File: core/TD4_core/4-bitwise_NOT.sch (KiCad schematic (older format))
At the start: 2 parts, among them U3 74HC04

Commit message: Decoder done (finally!)
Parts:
- renumbered C2 to C17, U3 to U17

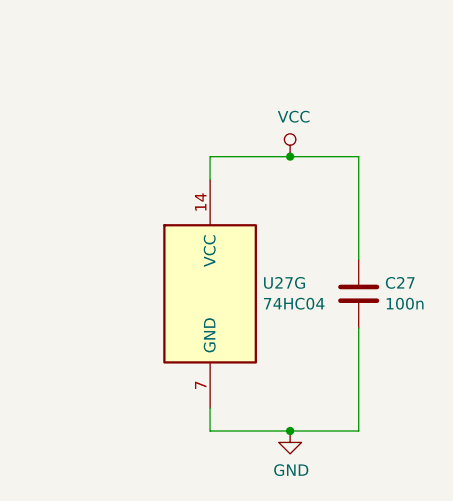
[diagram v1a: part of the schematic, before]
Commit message: Core schematic done. Backplane connector added, including separate .sch file to append.
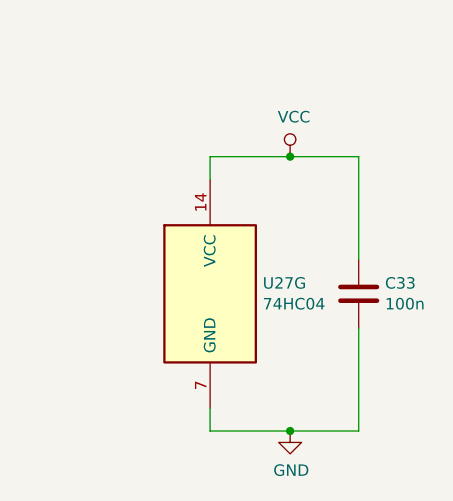
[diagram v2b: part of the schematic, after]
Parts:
- C23: renamed from C17; footprint (none) -> Capacitor_SMD:C_0805_2012Metric
- U17: footprint (none) -> Package_SO:SOIC-14_3.9x8.7mm_P1.27mm
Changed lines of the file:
@@
 encoding utf-8
 Sheet 6 23
-Title ""
+Title "TD4 core module"
 Date ""
-Rev ""
+Rev "v1.0"
 Comp ""
 Comment1 ""
@@
 F 0 "U27" H 5100 2617 50  0000 C CNN
 F 1 "74HC04" H 5100 2526 50  0000 C CNN
-F 2 "" H 5100 2300 50  0001 C CNN
+F 2 "Package_SO:SOIC-14_3.9x8.7mm_P1.27mm" H 5100 2300 50  0001 C CNN
 F 3 "http://www.nxp.com/documents/data_sheet/74HC_HCT04.pdf" H 5100 2300 50  0001 C CNN
 	1    5100 2300
@@
 F 0 "U27" H 5100 3117 50  0000 C CNN
 F 1 "74HC04" H 5100 3026 50  0000 C CNN
-F 2 "" H 5100 2800 50  0001 C CNN
+F 2 "Package_SO:SOIC-14_3.9x8.7mm_P1.27mm" H 5100 2800 50  0001 C CNN
 F 3 "http://www.nxp.com/documents/data_sheet/74HC_HCT04.pdf" H 5100 2800 50  0001 C CNN
 	2    5100 2800
@@
 F 0 "U27" H 5100 3617 50  0000 C CNN
 F 1 "74HC04" H 5100 3526 50  0000 C CNN
-F 2 "" H 5100 3300 50  0001 C CNN
+F 2 "Package_SO:SOIC-14_3.9x8.7mm_P1.27mm" H 5100 3300 50  0001 C CNN
 F 3 "http://www.nxp.com/documents/data_sheet/74HC_HCT04.pdf" H 5100 3300 50  0001 C CNN
 	3    5100 3300
@@
 F 0 "U27" H 5100 4117 50  0000 C CNN
 F 1 "74HC04" H 5100 4026 50  0000 C CNN
-F 2 "" H 5100 3800 50  0001 C CNN
+F 2 "Package_SO:SOIC-14_3.9x8.7mm_P1.27mm" H 5100 3800 50  0001 C CNN
 F 3 "http://www.nxp.com/documents/data_sheet/74HC_HCT04.pdf" H 5100 3800 50  0001 C CNN
 	4    5100 3800
@@
 F 0 "U27" H 5100 4617 50  0000 C CNN
 F 1 "74HC04" H 5100 4526 50  0000 C CNN
-F 2 "" H 5100 4300 50  0001 C CNN
+F 2 "Package_SO:SOIC-14_3.9x8.7mm_P1.27mm" H 5100 4300 50  0001 C CNN
 F 3 "http://www.nxp.com/documents/data_sheet/74HC_HCT04.pdf" H 5100 4300 50  0001 C CNN
 	5    5100 4300
@@
 F 0 "U27" H 5100 5117 50  0000 C CNN
 F 1 "74HC04" H 5100 5026 50  0000 C CNN
-F 2 "" H 5100 4800 50  0001 C CNN
+F 2 "Package_SO:SOIC-14_3.9x8.7mm_P1.27mm" H 5100 4800 50  0001 C CNN
 F 3 "http://www.nxp.com/documents/data_sheet/74HC_HCT04.pdf" H 5100 4800 50  0001 C CNN
 	6    5100 4800
@@
 F 0 "U27" H 8430 5646 50  0000 L CNN
 F 1 "74HC04" H 8430 5555 50  0000 L CNN
-F 2 "" H 8200 5600 50  0001 C CNN
+F 2 "Package_SO:SOIC-14_3.9x8.7mm_P1.27mm" H 8200 5600 50  0001 C CNN
 F 3 "http://www.nxp.com/documents/data_sheet/74HC_HCT04.pdf" H 8200 5600 50  0001 C CNN
 	7    8200 5600
@@
 AR Path="/5C5DC05E/5CD1F07F/5C820D48" Ref="C?"  Part="1"
 AR Path="/5C5DC05E/5CD1F083/5C820D48" Ref="C?"  Part="1"
-AR Path="/5C594F41/5C6679B7/5C820D48" Ref="C17"  Part="1"
+AR Path="/5C594F41/5C6679B7/5C820D48" Ref="C23"  Part="1"
 AR Path="/5C594F41/5C66DBE0/5C820D48" Ref="C?"  Part="1"
-AR Path="/5C594F41/5C66DBF5/5C820D48" Ref="C20"  Part="1"
-AR Path="/5C594F41/5C66DC0A/5C820D48" Ref="C22"  Part="1"
-AR Path="/5C594F41/5C66DC28/5C820D48" Ref="C24"  Part="1"
-AR Path="/5C594F41/5C67520B/5C820D48" Ref="C27"  Part="1"
+AR Path="/5C594F41/5C66DBF5/5C820D48" Ref="C26"  Part="1"
+AR Path="/5C594F41/5C66DC0A/5C820D48" Ref="C28"  Part="1"
+AR Path="/5C594F41/5C66DC28/5C820D48" Ref="C30"  Part="1"
+AR Path="/5C594F41/5C67520B/5C820D48" Ref="C33"  Part="1"
 AR Path="/5C594F41/5C691BDA/5C820D48" Ref="C?"  Part="1"
-F 0 "C27" H 8965 5646 50  0000 L CNN
+F 0 "C33" H 8965 5646 50  0000 L CNN
 F 1 "100n" H 8965 5555 50  0000 L CNN
-F 2 "" H 8888 5450 50  0001 C CNN
+F 2 "Capacitor_SMD:C_0805_2012Metric" H 8888 5450 50  0001 C CNN
 F 3 "~" H 8850 5600 50  0001 C CNN
 	1    8850 5600
@@
 AR Path="/5C5DC05E/5CD1F07F/5C820E22" Ref="#PWR?"  Part="1"
 AR Path="/5C5DC05E/5CD1F083/5C820E22" Ref="#PWR?"  Part="1"
-AR Path="/5C594F41/5C6679B7/5C820E22" Ref="#PWR060"  Part="1"
+AR Path="/5C594F41/5C6679B7/5C820E22" Ref="#PWR074"  Part="1"
 AR Path="/5C594F41/5C66DBE0/5C820E22" Ref="#PWR?"  Part="1"
-AR Path="/5C594F41/5C66DBF5/5C820E22" Ref="#PWR068"  Part="1"
-AR Path="/5C594F41/5C66DC0A/5C820E22" Ref="#PWR074"  Part="1"
-AR Path="/5C594F41/5C66DC28/5C820E22" Ref="#PWR080"  Part="1"
-AR Path="/5C594F41/5C67520B/5C820E22" Ref="#PWR088"  Part="1"
+AR Path="/5C594F41/5C66DBF5/5C820E22" Ref="#PWR082"  Part="1"
+AR Path="/5C594F41/5C66DC0A/5C820E22" Ref="#PWR088"  Part="1"
+AR Path="/5C594F41/5C66DC28/5C820E22" Ref="#PWR094"  Part="1"
+AR Path="/5C594F41/5C67520B/5C820E22" Ref="#PWR0102"  Part="1"
 AR Path="/5C594F41/5C691BDA/5C820E22" Ref="#PWR?"  Part="1"
-F 0 "#PWR088" H 8550 5950 50  0001 C CNN
+F 0 "#PWR0102" H 8550 5950 50  0001 C CNN
 F 1 "GND" H 8555 6027 50  0000 C CNN
 F 2 "" H 8550 6200 50  0001 C CNN
@@
 AR Path="/5C5DC05E/5CD1F07F/5C820E73" Ref="#PWR?"  Part="1"
 AR Path="/5C5DC05E/5CD1F083/5C820E73" Ref="#PWR?"  Part="1"
-AR Path="/5C594F41/5C6679B7/5C820E73" Ref="#PWR059"  Part="1"
+AR Path="/5C594F41/5C6679B7/5C820E73" Ref="#PWR073"  Part="1"
 AR Path="/5C594F41/5C66DBE0/5C820E73" Ref="#PWR?"  Part="1"
-AR Path="/5C594F41/5C66DBF5/5C820E73" Ref="#PWR067"  Part="1"
-AR Path="/5C594F41/5C66DC0A/5C820E73" Ref="#PWR073"  Part="1"
-AR Path="/5C594F41/5C66DC28/5C820E73" Ref="#PWR079"  Part="1"
-AR Path="/5C594F41/5C67520B/5C820E73" Ref="#PWR087"  Part="1"
+AR Path="/5C594F41/5C66DBF5/5C820E73" Ref="#PWR081"  Part="1"
+AR Path="/5C594F41/5C66DC0A/5C820E73" Ref="#PWR087"  Part="1"
+AR Path="/5C594F41/5C66DC28/5C820E73" Ref="#PWR093"  Part="1"
+AR Path="/5C594F41/5C67520B/5C820E73" Ref="#PWR0101"  Part="1"
 AR Path="/5C594F41/5C691BDA/5C820E73" Ref="#PWR?"  Part="1"
-F 0 "#PWR087" H 8550 4850 50  0001 C CNN
+F 0 "#PWR0101" H 8550 4850 50  0001 C CNN
 F 1 "VCC" H 8567 5173 50  0000 C CNN
 F 2 "" H 8550 5000 50  0001 C CNN
@@
 AR Path="/5C5DC05E/5CD1F07F/5C8210C3" Ref="#PWR?"  Part="1"
 AR Path="/5C5DC05E/5CD1F083/5C8210C3" Ref="#PWR?"  Part="1"
-AR Path="/5C594F41/5C6679B7/5C8210C3" Ref="#PWR057"  Part="1"
+AR Path="/5C594F41/5C6679B7/5C8210C3" Ref="#PWR071"  Part="1"
 AR Path="/5C594F41/5C66DBE0/5C8210C3" Ref="#PWR?"  Part="1"
-AR Path="/5C594F41/5C66DBF5/5C8210C3" Ref="#PWR065"  Part="1"
-AR Path="/5C594F41/5C66DC0A/5C8210C3" Ref="#PWR071"  Part="1"
-AR Path="/5C594F41/5C66DC28/5C8210C3" Ref="#PWR077"  Part="1"
-AR Path="/5C594F41/5C67520B/5C8210C3" Ref="#PWR085"  Part="1"
+AR Path="/5C594F41/5C66DBF5/5C8210C3" Ref="#PWR079"  Part="1"
+AR Path="/5C594F41/5C66DC0A/5C8210C3" Ref="#PWR085"  Part="1"
+AR Path="/5C594F41/5C66DC28/5C8210C3" Ref="#PWR091"  Part="1"
+AR Path="/5C594F41/5C67520B/5C8210C3" Ref="#PWR099"  Part="1"
 AR Path="/5C594F41/5C691BDA/5C8210C3" Ref="#PWR?"  Part="1"
-F 0 "#PWR085" H 4750 4100 50  0001 C CNN
+F 0 "#PWR099" H 4750 4100 50  0001 C CNN
 F 1 "GND" H 4755 4177 50  0000 C CNN
 F 2 "" H 4750 4350 50  0001 C CNN
@@
 AR Path="/5C5DC05E/5CD1F07F/5C8210FD" Ref="#PWR?"  Part="1"
 AR Path="/5C5DC05E/5CD1F083/5C8210FD" Ref="#PWR?"  Part="1"
-AR Path="/5C594F41/5C6679B7/5C8210FD" Ref="#PWR058"  Part="1"
+AR Path="/5C594F41/5C6679B7/5C8210FD" Ref="#PWR072"  Part="1"
 AR Path="/5C594F41/5C66DBE0/5C8210FD" Ref="#PWR?"  Part="1"
-AR Path="/5C594F41/5C66DBF5/5C8210FD" Ref="#PWR066"  Part="1"
-AR Path="/5C594F41/5C66DC0A/5C8210FD" Ref="#PWR072"  Part="1"
-AR Path="/5C594F41/5C66DC28/5C8210FD" Ref="#PWR078"  Part="1"
-AR Path="/5C594F41/5C67520B/5C8210FD" Ref="#PWR086"  Part="1"
+AR Path="/5C594F41/5C66DBF5/5C8210FD" Ref="#PWR080"  Part="1"
+AR Path="/5C594F41/5C66DC0A/5C8210FD" Ref="#PWR086"  Part="1"
+AR Path="/5C594F41/5C66DC28/5C8210FD" Ref="#PWR092"  Part="1"
+AR Path="/5C594F41/5C67520B/5C8210FD" Ref="#PWR0100"  Part="1"
 AR Path="/5C594F41/5C691BDA/5C8210FD" Ref="#PWR?"  Part="1"
-F 0 "#PWR086" H 4750 4600 50  0001 C CNN
+F 0 "#PWR0100" H 4750 4600 50  0001 C CNN
 F 1 "GND" H 4755 4677 50  0000 C CNN
 F 2 "" H 4750 4850 50  0001 C CNN
